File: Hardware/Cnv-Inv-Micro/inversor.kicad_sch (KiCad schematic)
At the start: 13 parts, among them Q1 TK8A65D, Q2 TK8A65D, Q3 TK8A65D, Q4 TK8A65D, Q5 TK8A65D, Q6 TK8A65D

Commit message: Normalizacion placa micros
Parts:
- added C15, C16: 4.7uF, Capacitor_SMD:CP_Elec_4x5.4, symbol Device:C_Polarized_Small
- added Inv_Pwr_A1: Conn_01x02, Connector_Molex:Molex_KK-254_AE-6410-02A_1x02_P2.54mm_Vertical, symbol Connector_Generic:Conn_01x02
- added U5: TMA-12012S-2WR3, Converter_DCDC:Converter_DCDC_TRACO_TMA-05xxS_12xxS_Single_THT, symbol Converter_DCDC:TMA-1205S
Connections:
- new net: C16.1, Inv_Pwr_A1.1 (Pin_1), U5.6 (+Vout)
- new net: C16.2, Inv_Pwr_A1.2 (Pin_2), U5.4 (-Vout)
- new net 12V_Cnv: C15.1, U5.1 (+Vin)
- new net Gnd_Cnv: C15.2, U5.2 (-Vin)

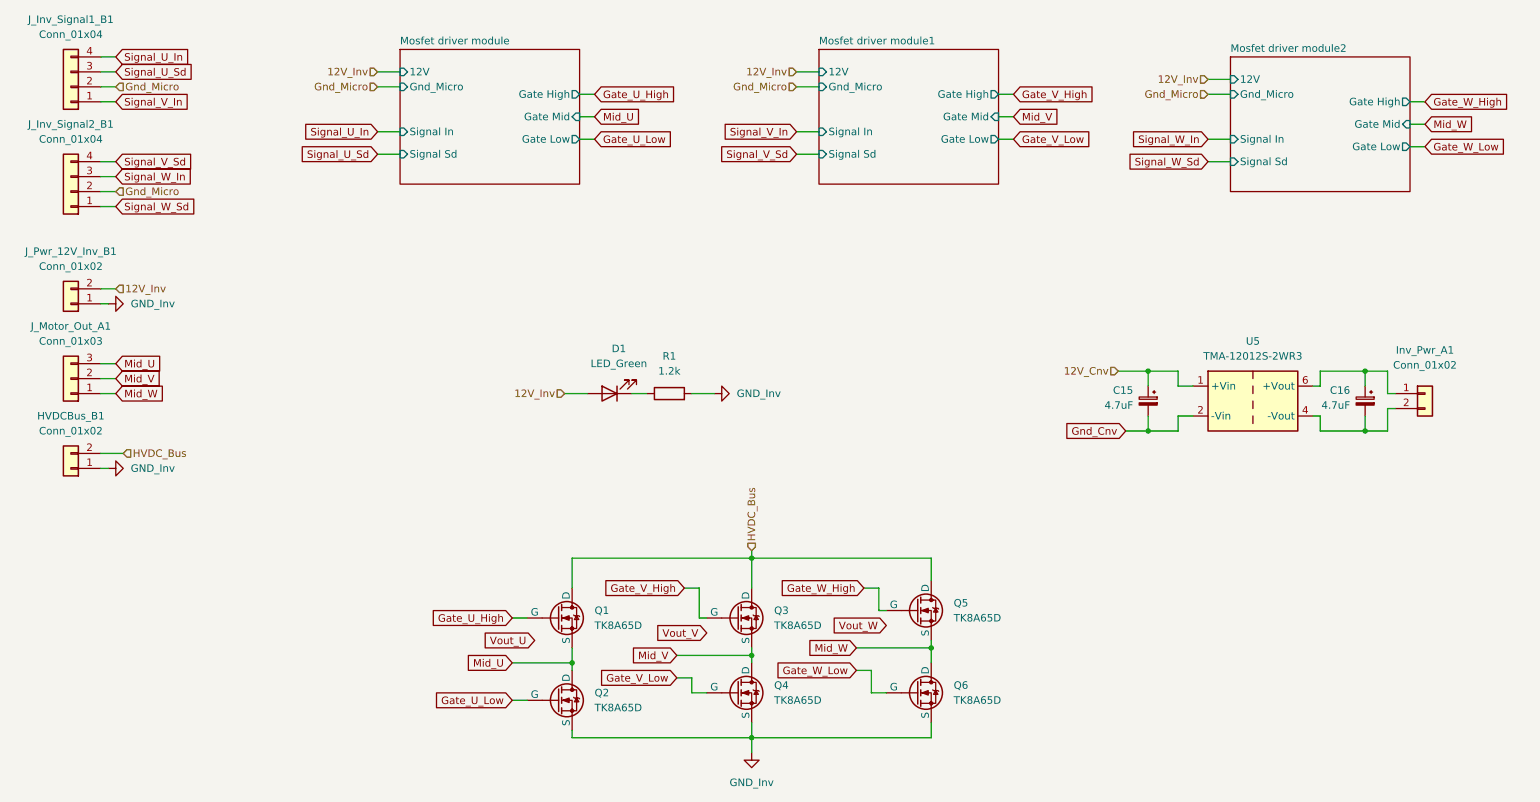
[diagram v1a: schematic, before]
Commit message: Avances en PCB conversor y inversor - Simulaciones de modulacion
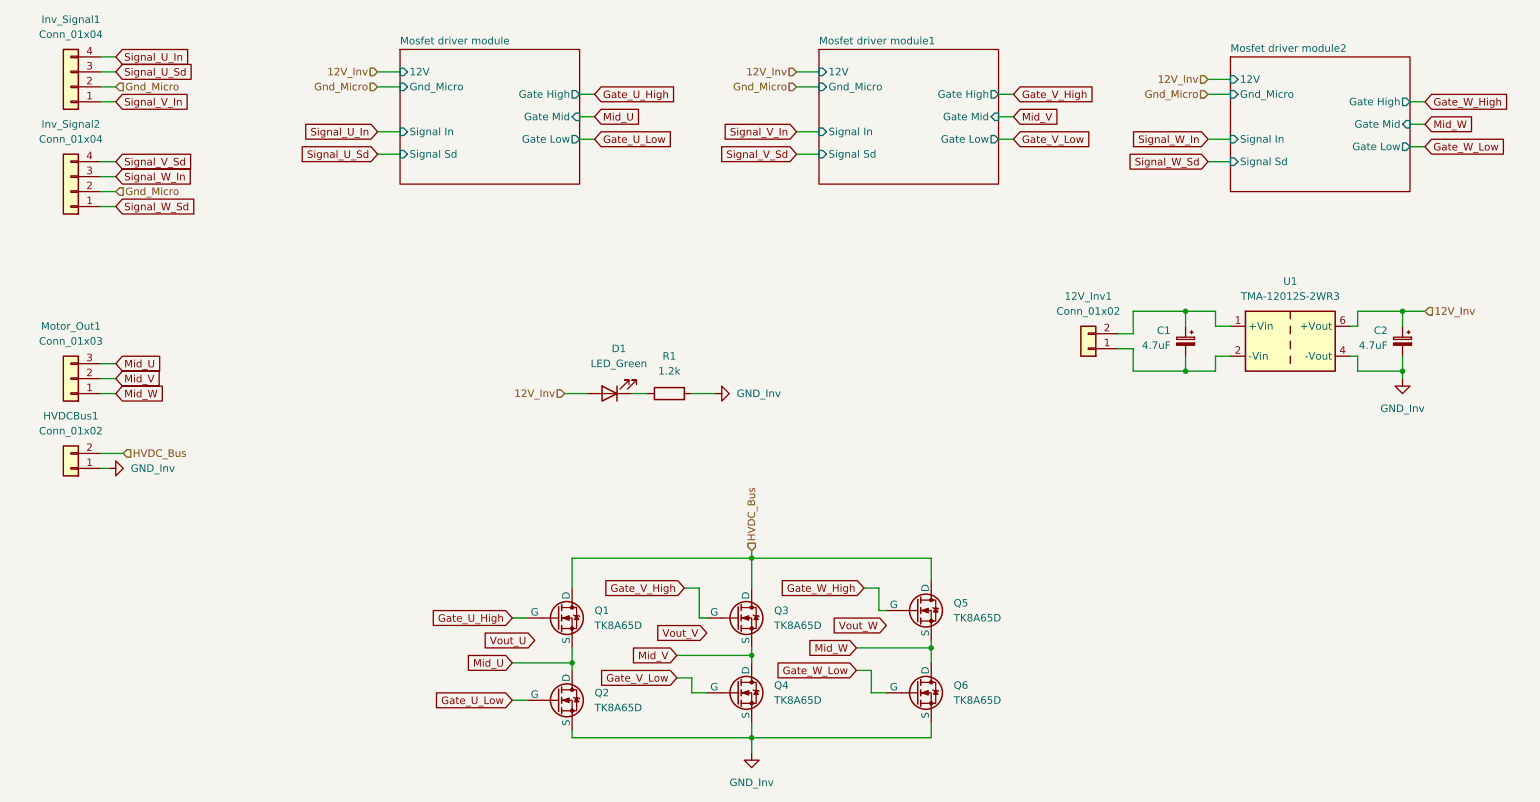
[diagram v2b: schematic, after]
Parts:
- removed Inv_Pwr_A1: Conn_01x02, Connector_Molex:Molex_KK-254_AE-6410-02A_1x02_P2.54mm_Vertical, symbol Connector_Generic:Conn_01x02
- renumbered J_Pwr_12V_Inv_B1 to 12V_Inv1, C15 to C1, C16 to C2, HVDCBus_B1 to HVDCBus1, J_Inv_Signal1_B1 to Inv_Signal1, J_Inv_Signal2_B1 to Inv_Signal2, J_Motor_Out_A1 to Motor_Out1, U5 to U1
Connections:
- net 12V_Inv: now also C2.1, U1.6 (+Vout); no longer 12V_Inv1.2 (Pin_2)
- net GND_Inv: now also C2.2, U1.4 (-Vout); no longer 12V_Inv1.1 (Pin_1)
- net 12V_Cnv: no longer names the net of C1.1, U1.1 (+Vin)
- net 12V_Cnv: now also 12V_Inv1.2 (Pin_2)
- net Gnd_Cnv: no longer names the net of C1.2, U1.2 (-Vin)
- net Gnd_Cnv: now also 12V_Inv1.1 (Pin_1)
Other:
- moved on the sheet: 12V_Inv1, C1, C2, U1
